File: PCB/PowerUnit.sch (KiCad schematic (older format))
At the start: 135 parts, among them J1 MX150-20, J2 MX150-20, J3 MX150-8, J4 REDCUBE, J5 CON-3, Q1 BC847C, Q10 STD45P4LLF6AG, Q11 STD45P4LLF6AG, Q12 STD15P6F6AG, Q13 STD15P6F6AG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

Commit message: fix Fab
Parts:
- C10, C11, C12, C13, C2, C3, C5, C6, C7, C8: value 10n -> 100n; ItemNo 220200 -> 220250
- R1, R14, R15, R16, R19, R2, R20, R24, R25, R26, R27, R3, R39, R4, R8: value 2.2k -> 1k; ItemNo 200766 -> 200750
- R10, R11, R12, R17, R18, R21, R22, R23, R7, R9: value 820 -> 1k; ItemNo 200744 -> 200750

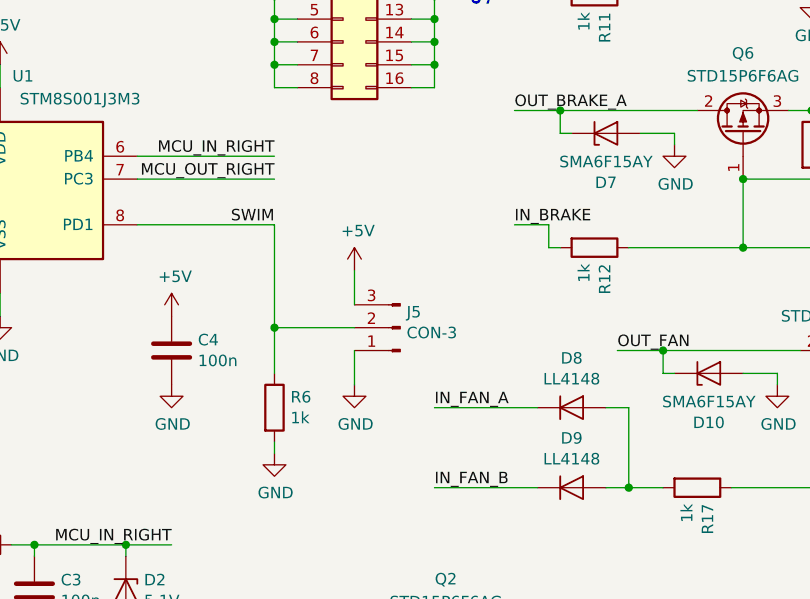
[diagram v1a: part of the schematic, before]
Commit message: Changed debug connector
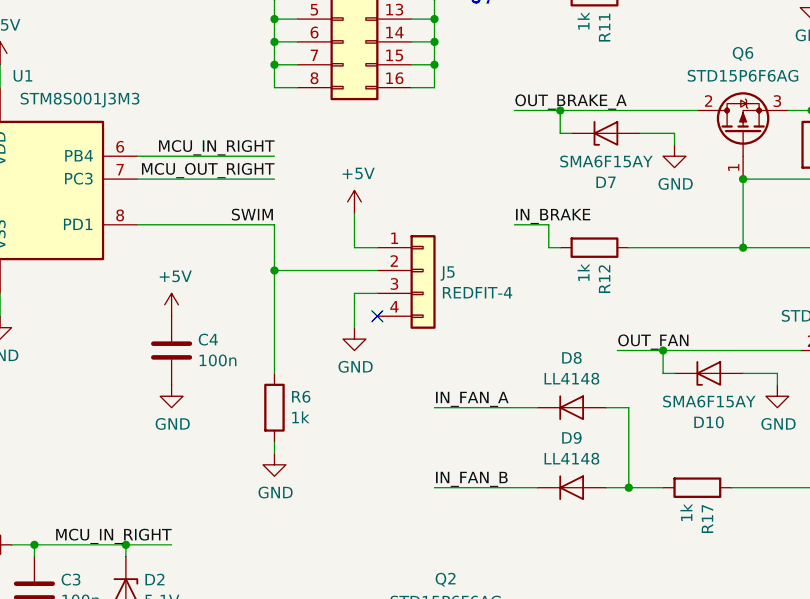
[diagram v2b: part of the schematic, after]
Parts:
- removed J5: CON-3, erp:PinHeader_1x03_P2.54mm_Vertical, symbol erp:Conn_01x03_Male
- added J5: REDFIT-4, symbol erp:Conn_01x04
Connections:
- net +5V: now also J5.1 (Pin_1)
- net GND: now also J5.3 (Pin_3)
- net SWIM: now also J5.2 (Pin_2)
- no-connect marks 3 -> 4
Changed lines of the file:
@@
 EESchema Schematic File Version 4
-LIBS:PowerUnit-cache
 EELAYER 30 0
 EELAYER END
@@
 	1    0    0    -1
 $EndComp
-$Comp
-L erp:Conn_01x03_Male J5
-U 1 1 5E35D565
-P 3500 5200
-F 0 "J5" H 3472 5132 50  0000 R CNN
-F 1 "CON-3" H 3472 5223 50  0000 R CNN
-F 2 "erp:PinHeader_1x03_P2.54mm_Vertical" H 3500 5200 50  0001 C CNN
-F 3 "" H 3500 5200 50  0001 C CNN
-F 4 "501002" H 3500 5200 50  0001 C CNN "ItemNo"
-	1    3500 5200
-	-1   0    0    1
-$EndComp
 Wire Wire Line
-	2950 4750 2950 5200
+	2950 4750 2950 4950
 $Comp
 L power:GND #PWR0101
 U 1 1 5E5CCC11
-P 3300 5450
-F 0 "#PWR0101" H 3300 5200 50  0001 C CNN
-F 1 "GND" H 3305 5277 50  0000 C CNN
-F 2 "" H 3300 5450 50  0001 C CNN
-F 3 "" H 3300 5450 50  0001 C CNN
-	1    3300 5450
+P 3300 5200
+F 0 "#PWR0101" H 3300 4950 50  0001 C CNN
+F 1 "GND" H 3305 5027 50  0000 C CNN
+F 2 "" H 3300 5200 50  0001 C CNN
+F 3 "" H 3300 5200 50  0001 C CNN
+	1    3300 5200
 	1    0    0    -1
 $EndComp
@@
 L power:+5V #PWR0102
 U 1 1 5E670EE6
-P 3300 4950
-F 0 "#PWR0102" H 3300 4800 50  0001 C CNN
-F 1 "+5V" H 3315 5123 50  0000 C CNN
-F 2 "" H 3300 4950 50  0001 C CNN
-F 3 "" H 3300 4950 50  0001 C CNN
-	1    3300 4950
+P 3300 4700
+F 0 "#PWR0102" H 3300 4550 50  0001 C CNN
+F 1 "+5V" H 3315 4873 50  0000 C CNN
+F 2 "" H 3300 4700 50  0001 C CNN
+F 3 "" H 3300 4700 50  0001 C CNN
+	1    3300 4700
 	1    0    0    -1
 $EndComp
 Wire Wire Line
-	3300 5300 3300 5450
+	3300 5050 3300 5200
 Wire Wire Line
-	3300 4950 3300 5100
-Wire Wire Line
-	2950 5200 3300 5200
-Wire Wire Line
-	2950 5200 2950 5400
-Connection ~ 2950 5200
+	3300 4700 3300 4850
 $Comp
 L erp:Conn_02x08_Top_Bottom J4
@@
 	0    1    1    0
 $EndComp
+$Comp
+L erp:Conn_01x04 J5
+U 1 1 5E8BDB9D
+P 3600 4950
+F 0 "J5" H 3680 4942 50  0000 L CNN
+F 1 "REDFIT-4" H 3680 4851 50  0000 L CNN
+F 2 "" H 3600 4950 50  0001 C CNN
+F 3 "" H 3600 4950 50  0001 C CNN
+F 4 "502001" H 3600 4950 50  0001 C CNN "ItemNo"
+	1    3600 4950
+	1    0    0    -1
+$EndComp
+Connection ~ 2950 4950
+Wire Wire Line
+	2950 4950 2950 5400
+NoConn ~ 3400 5150
+Wire Wire Line
+	3400 5050 3300 5050
+Wire Wire Line
+	2950 4950 3400 4950
+Wire Wire Line
+	3400 4850 3300 4850
 $EndSCHEMATC
